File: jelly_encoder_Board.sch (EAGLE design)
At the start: 3 parts, among them IC1 IC-MU150_DFN16-5X5, J1 SM05B-SRSS-TB(LF)(SN)

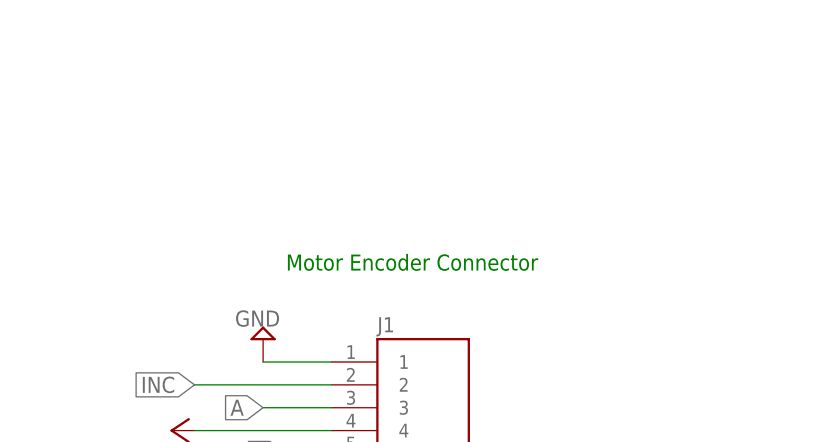
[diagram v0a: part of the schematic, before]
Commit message: added second connector for JST-PH and fixed routes
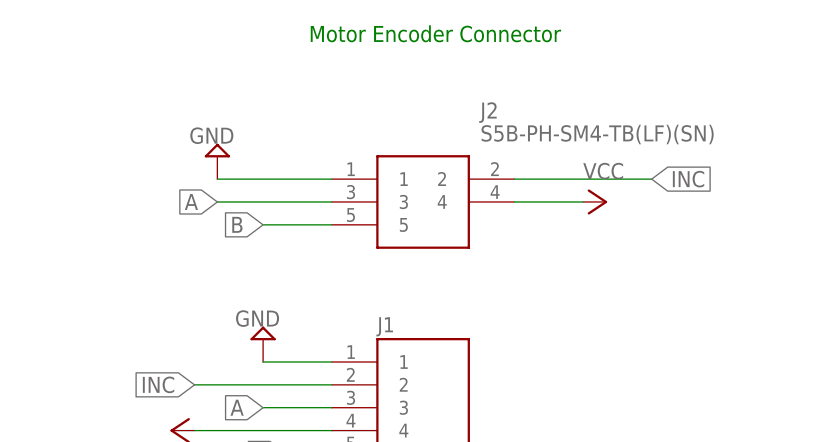
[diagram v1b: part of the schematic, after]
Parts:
- added J2: S5B-PH-SM4-TB(LF)(SN), S5B-PH-SM4-TB(LF)(SN):S5B-PH-SM4-TB(LF)(SN)
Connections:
- net A: now also J2.3
- net B: now also J2.5
- net GND: now also J2.1
- net INC: now also J2.2
- net VCC: now also J2.4
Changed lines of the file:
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@@
 <part name="P+4" library="supply1" library_urn="urn:adsk.eagle:library:371" deviceset="VCC" device=""/>
 <part name="JP1" library="pinhead" library_urn="urn:adsk.eagle:library:325" deviceset="PINHD-1X11" device="/90" package3d_urn="urn:adsk.eagle:package:22416/2"/>
+<part name="J2" library="S5B-PH-SM4-TB(LF)(SN)" deviceset="S5B-PH-SM4-TB(LF)(SN)" device=""/>
+<part name="P+5" library="supply1" library_urn="urn:adsk.eagle:library:371" deviceset="VCC" device=""/>
+<part name="SUPPLY7" library="supply2" library_urn="urn:adsk.eagle:library:372" deviceset="GND" device=""/>
 </parts>
 <sheets>
 <sheet>
 <plain>
-<text x="96.52" y="86.36" size="1.778" layer="91">Motor Encoder Connector</text>
+<text x="99.06" y="111.76" size="1.778" layer="91">Motor Encoder Connector</text>
 <text x="12.7" y="91.44" size="1.778" layer="91">Motor Encoder</text>
 <text x="93.98" y="45.72" size="1.778" layer="91">Motor Encoder Programmer</text>
@@
 <instance part="P+4" gate="VCC" x="0" y="93.98"/>
 <instance part="JP1" gate="A" x="114.3" y="22.86"/>
+<instance part="J2" gate="G$1" x="101.6" y="96.52"/>
+<instance part="P+5" gate="VCC" x="132.08" y="93.98" rot="R270"/>
+<instance part="SUPPLY7" gate="GND" x="88.9" y="99.06" rot="R180"/>
 </instances>
 <busses>
@@
 <wire x1="101.6" y1="76.2" x2="93.98" y2="76.2" width="0.1524" layer="91"/>
 </segment>
+<segment>
+<pinref part="SUPPLY7" gate="GND" pin="GND"/>
+<wire x1="101.6" y1="96.52" x2="88.9" y2="96.52" width="0.1524" layer="91"/>
+<pinref part="J2" gate="G$1" pin="1"/>
+</segment>
 </net>
 <net name="VCC" class="0">
@@
 <wire x1="101.6" y1="68.58" x2="86.36" y2="68.58" width="0.1524" layer="91"/>
 </segment>
+<segment>
+<pinref part="P+5" gate="VCC" pin="VCC"/>
+<wire x1="121.92" y1="93.98" x2="129.54" y2="93.98" width="0.1524" layer="91"/>
+<pinref part="J2" gate="G$1" pin="4"/>
+</segment>
 </net>
 <net name="A" class="0">
@@
 <wire x1="101.6" y1="71.12" x2="93.98" y2="71.12" width="0.1524" layer="91"/>
 <label x="93.98" y="71.12" size="1.778" layer="95" rot="R180" xref="yes"/>
+</segment>
+<segment>
+<wire x1="101.6" y1="93.98" x2="88.9" y2="93.98" width="0.1524" layer="91"/>
+<label x="88.9" y="93.98" size="1.778" layer="95" rot="R180" xref="yes"/>
+<pinref part="J2" gate="G$1" pin="3"/>
 </segment>
 </net>
@@
 <label x="96.52" y="66.04" size="1.778" layer="95" rot="R180" xref="yes"/>
 </segment>
+<segment>
+<wire x1="101.6" y1="91.44" x2="93.98" y2="91.44" width="0.1524" layer="91"/>
+<label x="93.98" y="91.44" size="1.778" layer="95" rot="R180" xref="yes"/>
+<pinref part="J2" gate="G$1" pin="5"/>
+</segment>
 </net>
 <net name="INC" class="0">
@@
 <label x="86.36" y="73.66" size="1.778" layer="95" rot="R180" xref="yes"/>
 </segment>
+<segment>
+<wire x1="121.92" y1="96.52" x2="137.16" y2="96.52" width="0.1524" layer="91"/>
+<label x="137.16" y="96.52" size="1.778" layer="95" xref="yes"/>
+<pinref part="J2" gate="G$1" pin="2"/>
+</segment>
 </net>

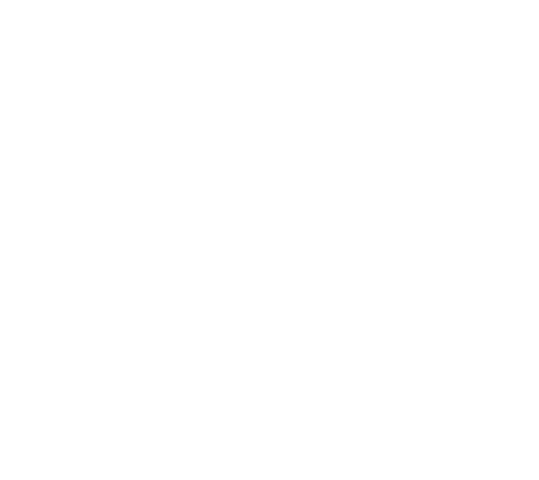
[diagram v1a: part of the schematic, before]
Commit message: added RGB Sensor pins
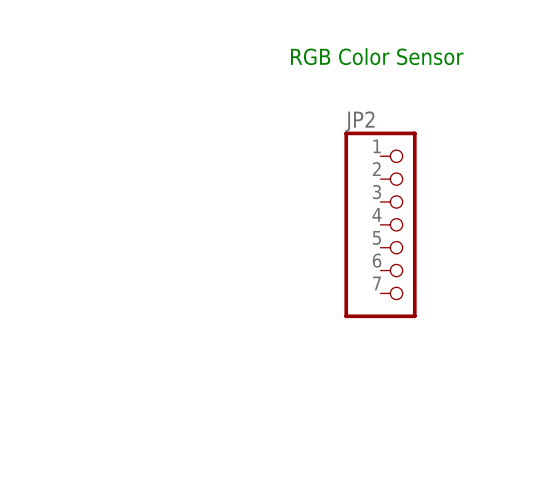
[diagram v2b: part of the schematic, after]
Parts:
- added JP2: (no value), pinhead:PINHD-1X7/90
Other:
- note added: "RGB Color Sensor"
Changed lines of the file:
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@@
 <part name="P+5" library="supply1" library_urn="urn:adsk.eagle:library:371" deviceset="VCC" device=""/>
 <part name="SUPPLY7" library="supply2" library_urn="urn:adsk.eagle:library:372" deviceset="GND" device=""/>
+<part name="JP2" library="pinhead" library_urn="urn:adsk.eagle:library:325" deviceset="PINHD-1X7" device="/90" package3d_urn="urn:adsk.eagle:package:22476/2"/>
 </parts>
 <sheets>
@@
 <text x="12.7" y="91.44" size="1.778" layer="91">Motor Encoder</text>
 <text x="93.98" y="45.72" size="1.778" layer="91">Motor Encoder Programmer</text>
+<text x="182.88" y="109.22" size="1.778" layer="91">RGB Color Sensor</text>
 </plain>
 <instances>
@@
 <instance part="P+5" gate="VCC" x="132.08" y="93.98" rot="R270"/>
 <instance part="SUPPLY7" gate="GND" x="88.9" y="99.06" rot="R180"/>
+<instance part="JP2" gate="A" x="195.58" y="91.44"/>
 </instances>
 <busses>

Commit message: fixed traces and added decoupling caps
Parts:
- added C1, C2: .1uF, resistor:C-USC0603
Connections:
- net GND: now also C1.2, C2.2
- net VCC: now also C1.1, C2.1
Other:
- moved on the sheet: JP2
